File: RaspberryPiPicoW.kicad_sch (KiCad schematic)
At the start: 2 parts, among them U1 Raspberry Pi Pico W

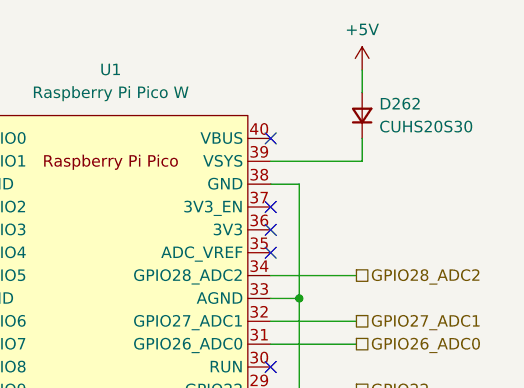
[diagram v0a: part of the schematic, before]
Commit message: 外周LEDを116個に修正
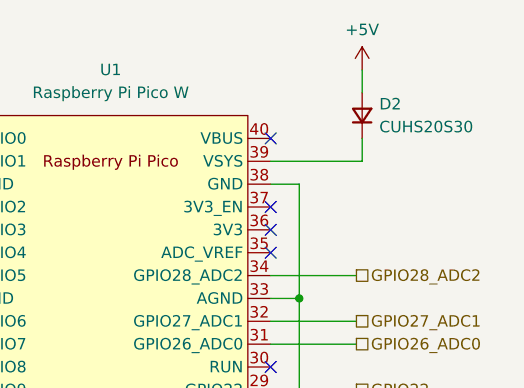
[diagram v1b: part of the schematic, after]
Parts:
- renumbered D262 to D2
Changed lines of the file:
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@@
 		(dnp no)
 		(fields_autoplaced yes)
-		(property "Reference" "#PWR062"
+		(property "Reference" "#PWR09"
 			(at 169.545 133.35 0)
 			(effects
@@
 		(dnp no)
 		(fields_autoplaced yes)
-		(property "Reference" "D262"
+		(property "Reference" "D2"
 			(at 178.435 72.39 90)
 			(effects
@@
 		(dnp no)
 		(fields_autoplaced yes)
-		(property "Reference" "#PWR061"
+		(property "Reference" "#PWR08"
 			(at 128.27 133.35 0)
 			(effects
@@
 		(dnp no)
 		(fields_autoplaced yes)
-		(property "Reference" "#PWR063"
+		(property "Reference" "#PWR010"
 			(at 176.53 72.39 0)
 			(effects
